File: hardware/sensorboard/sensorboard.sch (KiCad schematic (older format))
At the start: 25 parts, among them P1 PWR, P2 PROG, U1 ESP-07v2, U2 LMR16006Y, U3 BME280

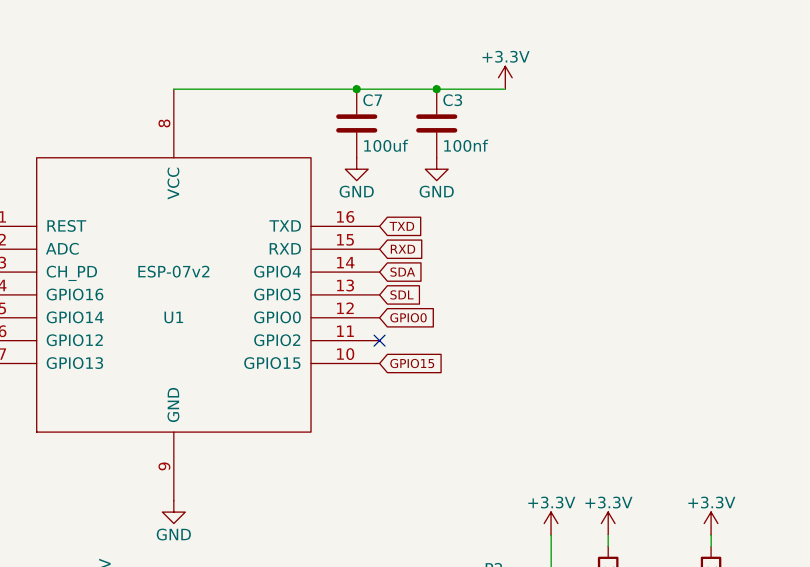
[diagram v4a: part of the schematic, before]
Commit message: Fix sensor placement and improve silkscreens
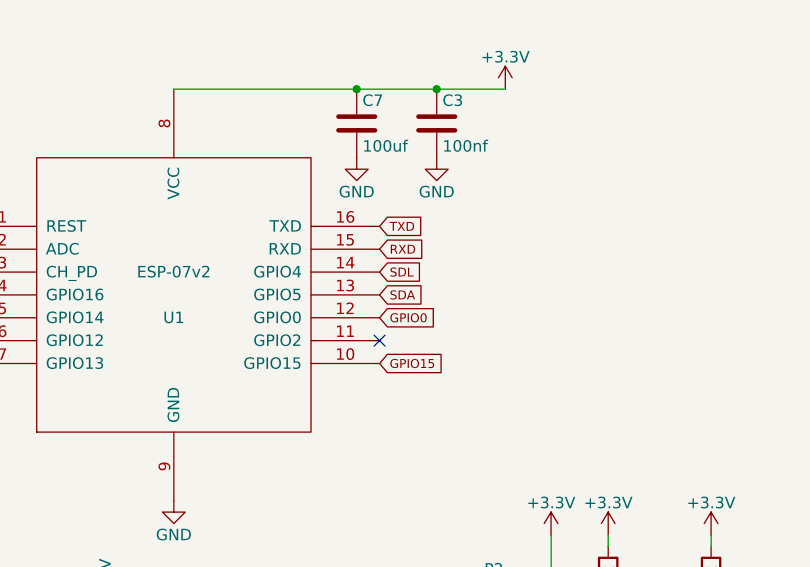
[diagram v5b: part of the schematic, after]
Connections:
- net SDA: now also U1.13 (GPIO5); no longer U1.14 (GPIO4)
- net SDL: now also U1.14 (GPIO4); no longer U1.13 (GPIO5)
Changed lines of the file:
@@
 $EndComp
 $Comp
-L GND #PWR22
+L GND #PWR01
 U 1 1 55FE3581
 P 3350 2700
-F 0 "#PWR22" H 3350 2450 50  0001 C CNN
+F 0 "#PWR01" H 3350 2450 50  0001 C CNN
 F 1 "GND" H 3350 2550 50  0000 C CNN
 F 2 "" H 3350 2700 60  0000 C CNN
@@
 $EndComp
 $Comp
-L +6V #PWR1
+L +6V #PWR02
 U 1 1 55FE36BB
 P 600 5000
-F 0 "#PWR1" H 600 4850 50  0001 C CNN
+F 0 "#PWR02" H 600 4850 50  0001 C CNN
 F 1 "+6V" H 600 5140 50  0000 C CNN
 F 2 "" H 600 5000 60  0000 C CNN
@@
 $EndComp
 $Comp
-L GND #PWR2
+L GND #PWR03
 U 1 1 55FE36DF
 P 600 5100
-F 0 "#PWR2" H 600 4850 50  0001 C CNN
+F 0 "#PWR03" H 600 4850 50  0001 C CNN
 F 1 "GND" H 600 4950 50  0000 C CNN
 F 2 "" H 600 5100 60  0000 C CNN
@@
 $EndComp
 $Comp
-L GND #PWR7
+L GND #PWR04
 U 1 1 55FE3994
 P 1300 600
-F 0 "#PWR7" H 1300 350 50  0001 C CNN
+F 0 "#PWR04" H 1300 350 50  0001 C CNN
 F 1 "GND" H 1300 450 50  0000 C CNN
 F 2 "" H 1300 600 60  0000 C CNN
@@
 $EndComp
 $Comp
-L +3.3V #PWR28
+L +3.3V #PWR05
 U 1 1 55FE3BCB
 P 4800 900
-F 0 "#PWR28" H 4800 750 50  0001 C CNN
+F 0 "#PWR05" H 4800 750 50  0001 C CNN
 F 1 "+3.3V" H 4800 1040 50  0000 C CNN
 F 2 "" H 4800 900 60  0000 C CNN
@@
 $EndComp
 $Comp
-L GND #PWR26
+L GND #PWR06
 U 1 1 55FE3BE8
 P 4500 1200
-F 0 "#PWR26" H 4500 950 50  0001 C CNN
+F 0 "#PWR06" H 4500 950 50  0001 C CNN
 F 1 "GND" H 4500 1050 50  0000 C CNN
 F 2 "" H 4500 1200 60  0000 C CNN
@@
 CH_PD
 $Comp
-L +3.3V #PWR19
+L +3.3V #PWR07
 U 1 1 55FE58BB
 P 3050 3200
-F 0 "#PWR19" H 3050 3050 50  0001 C CNN
+F 0 "#PWR07" H 3050 3050 50  0001 C CNN
 F 1 "+3.3V" V 3050 3340 50  0000 C CNN
 F 2 "" H 3050 3200 60  0000 C CNN
@@
 $EndComp
 $Comp
-L GND #PWR21
+L GND #PWR08
 U 1 1 55FE59ED
 P 3300 3650
-F 0 "#PWR21" H 3300 3400 50  0001 C CNN
+F 0 "#PWR08" H 3300 3400 50  0001 C CNN
 F 1 "GND" H 3300 3500 50  0000 C CNN
 F 2 "" H 3300 3650 60  0000 C CNN
@@
 RXD
 $Comp
-L GND #PWR27
+L GND #PWR09
 U 1 1 55FF1EBD
 P 4500 3500
-F 0 "#PWR27" H 4500 3250 50  0001 C CNN
+F 0 "#PWR09" H 4500 3250 50  0001 C CNN
 F 1 "GND" H 4500 3350 50  0000 C CNN
 F 2 "" H 4500 3500 60  0000 C CNN
@@
 $EndComp
 $Comp
-L +3.3V #PWR29
+L +3.3V #PWR010
 U 1 1 55FF1FBC
 P 5000 2850
-F 0 "#PWR29" H 5000 2700 50  0001 C CNN
+F 0 "#PWR010" H 5000 2700 50  0001 C CNN
 F 1 "+3.3V" H 5000 2990 50  0000 C CNN
 F 2 "" H 5000 2850 60  0000 C CNN
@@
 $EndComp
 $Comp
-L +3.3V #PWR30
+L +3.3V #PWR011
 U 1 1 55FF2085
 P 5250 2850
-F 0 "#PWR30" H 5250 2700 50  0001 C CNN
+F 0 "#PWR011" H 5250 2700 50  0001 C CNN
 F 1 "+3.3V" H 5250 2990 50  0000 C CNN
 F 2 "" H 5250 2850 60  0000 C CNN
@@
 $EndComp
 $Comp
-L +3.3V #PWR31
+L +3.3V #PWR012
 U 1 1 55FF24C3
 P 5700 2850
-F 0 "#PWR31" H 5700 2700 50  0001 C CNN
+F 0 "#PWR012" H 5700 2700 50  0001 C CNN
 F 1 "+3.3V" H 5700 2990 50  0000 C CNN
 F 2 "" H 5700 2850 60  0000 C CNN
@@
 ADC_IN
 $Comp
-L GND #PWR12
+L GND #PWR013
 U 1 1 562D40D4
 P 1950 1250
-F 0 "#PWR12" H 1950 1000 50  0001 C CNN
+F 0 "#PWR013" H 1950 1000 50  0001 C CNN
 F 1 "GND" H 1950 1100 50  0000 C CNN
 F 2 "" H 1950 1250 60  0000 C CNN
@@
 $EndComp
 $Comp
-L +6V #PWR11
+L +6V #PWR014
 U 1 1 562D410C
 P 1950 650
-F 0 "#PWR11" H 1950 500 50  0001 C CNN
+F 0 "#PWR014" H 1950 500 50  0001 C CNN
 F 1 "+6V" H 1950 790 50  0000 C CNN
 F 2 "" H 1950 650 60  0000 C CNN
@@
 $EndComp
 $Comp
-L GND #PWR17
+L GND #PWR015
 U 1 1 56D21A8C
 P 2300 5000
-F 0 "#PWR17" H 2300 4750 50  0001 C CNN
+F 0 "#PWR015" H 2300 4750 50  0001 C CNN
 F 1 "GND" H 2300 4850 50  0000 C CNN
 F 2 "" H 2300 5000 60  0000 C CNN
@@
 $EndComp
 $Comp
-L GND #PWR3
+L GND #PWR016
 U 1 1 56D21D41
 P 900 5700
-F 0 "#PWR3" H 900 5450 50  0001 C CNN
+F 0 "#PWR016" H 900 5450 50  0001 C CNN
 F 1 "GND" H 900 5550 50  0000 C CNN
 F 2 "" H 900 5700 60  0000 C CNN
@@
 $EndComp
 $Comp
-L GND #PWR18
+L GND #PWR017
 U 1 1 56D2214B
 P 2600 5000
-F 0 "#PWR18" H 2600 4750 50  0001 C CNN
+F 0 "#PWR017" H 2600 4750 50  0001 C CNN
 F 1 "GND" H 2600 4850 50  0000 C CNN
 F 2 "" H 2600 5000 60  0000 C CNN
@@
 $EndComp
 $Comp
-L +3.3V #PWR24
+L +3.3V #PWR018
 U 1 1 56D22840
 P 3650 4700
-F 0 "#PWR24" H 3650 4550 50  0001 C CNN
+F 0 "#PWR018" H 3650 4550 50  0001 C CNN
 F 1 "+3.3V" H 3650 4840 50  0000 C CNN
 F 2 "" H 3650 4700 60  0000 C CNN
@@
 $EndComp
 $Comp
-L GND #PWR23
+L GND #PWR019
 U 1 1 56D228E6
 P 3450 5000
-F 0 "#PWR23" H 3450 4750 50  0001 C CNN
+F 0 "#PWR019" H 3450 4750 50  0001 C CNN
 F 1 "GND" H 3450 4850 50  0000 C CNN
 F 2 "" H 3450 5000 60  0000 C CNN
@@
 $EndComp
 $Comp
-L GND #PWR20
+L GND #PWR020
 U 1 1 56D22C06
 P 3100 5500
-F 0 "#PWR20" H 3100 5250 50  0001 C CNN
+F 0 "#PWR020" H 3100 5250 50  0001 C CNN
 F 1 "GND" H 3100 5350 50  0000 C CNN
 F 2 "" H 3100 5500 60  0000 C CNN
@@
 $EndComp
 NoConn ~ 2450 2100
+Text GLabel 4250 1800 2    39   Input ~ 0
+SDA
 Text GLabel 4250 1700 2    39   Input ~ 0
-SDA
-Text GLabel 4250 1800 2    39   Input ~ 0
 SDL
 Text GLabel 2450 1800 0    39   Input ~ 0
@@
 $EndComp
 $Comp
-L GND #PWR9
+L GND #PWR021
 U 1 1 570209C8
 P 1600 3650
-F 0 "#PWR9" H 1600 3400 50  0001 C CNN
+F 0 "#PWR021" H 1600 3400 50  0001 C CNN
 F 1 "GND" H 1600 3500 50  0000 C CNN
 F 2 "" H 1600 3650 60  0000 C CNN
@@
 $EndComp
 $Comp
-L GND #PWR14
+L GND #PWR022
 U 1 1 57020ED6
 P 2000 3650
-F 0 "#PWR14" H 2000 3400 50  0001 C CNN
+F 0 "#PWR022" H 2000 3400 50  0001 C CNN
 F 1 "GND" H 2000 3500 50  0000 C CNN
 F 2 "" H 2000 3650 60  0000 C CNN
@@
 $EndComp
 $Comp
-L +3.3V #PWR4
+L +3.3V #PWR023
 U 1 1 57021047
 P 1000 3950
-F 0 "#PWR4" H 1000 3800 50  0001 C CNN
+F 0 "#PWR023" H 1000 3800 50  0001 C CNN
 F 1 "+3.3V" V 1000 4090 50  0000 C CNN
 F 2 "" H 1000 3950 60  0000 C CNN
@@
 $EndComp
 $Comp
-L +3.3V #PWR16
+L +3.3V #PWR024
 U 1 1 57021094
 P 2300 3950
-F 0 "#PWR16" H 2300 3800 50  0001 C CNN
+F 0 "#PWR024" H 2300 3800 50  0001 C CNN
 F 1 "+3.3V" V 2300 4090 50  0000 C CNN
 F 2 "" H 2300 3950 60  0000 C CNN
@@
 $EndComp
 $Comp
-L +3.3V #PWR8
+L +3.3V #PWR025
 U 1 1 570216D8
 P 1600 2450
-F 0 "#PWR8" H 1600 2300 50  0001 C CNN
+F 0 "#PWR025" H 1600 2300 50  0001 C CNN
 F 1 "+3.3V" V 1600 2590 50  0000 C CNN
 F 2 "" H 1600 2450 60  0000 C CNN
@@
 $EndComp
 $Comp
-L GND #PWR6
+L GND #PWR026
 U 1 1 57021725
 P 1200 2650
-F 0 "#PWR6" H 1200 2400 50  0001 C CNN
+F 0 "#PWR026" H 1200 2400 50  0001 C CNN
 F 1 "GND" H 1200 2500 50  0000 C CNN
 F 2 "" H 1200 2650 60  0000 C CNN
@@
 SDL
 $Comp
-L +3.3V #PWR10
+L +3.3V #PWR027
 U 1 1 57021EEC
 P 1800 1900
-F 0 "#PWR10" H 1800 1750 50  0001 C CNN
+F 0 "#PWR027" H 1800 1750 50  0001 C CNN
 F 1 "+3.3V" V 1800 2040 50  0000 C CNN
 F 2 "" H 1800 1900 60  0000 C CNN
@@
 $EndComp
 $Comp
-L +3.3V #PWR13
+L +3.3V #PWR028
 U 1 1 57021F6F
 P 2000 1900
-F 0 "#PWR13" H 2000 1750 50  0001 C CNN
+F 0 "#PWR028" H 2000 1750 50  0001 C CNN
 F 1 "+3.3V" V 2000 2040 50  0000 C CNN
 F 2 "" H 2000 1900 60  0000 C CNN
@@
 Connection ~ 2000 2150
 $Comp
-L GND #PWR5
+L GND #PWR029
 U 1 1 57022E9C
 P 1150 4150
-F 0 "#PWR5" H 1150 3900 50  0001 C CNN
+F 0 "#PWR029" H 1150 3900 50  0001 C CNN
 F 1 "GND" H 1150 4000 50  0000 C CNN
 F 2 "" H 1150 4150 60  0000 C CNN
@@
 Connection ~ 2150 3950
 $Comp
-L GND #PWR15
+L GND #PWR030
 U 1 1 5702315A
 P 2150 4150
-F 0 "#PWR15" H 2150 3900 50  0001 C CNN
+F 0 "#PWR030" H 2150 3900 50  0001 C CNN
 F 1 "GND" H 2150 4000 50  0000 C CNN
 F 2 "" H 2150 4150 60  0000 C CNN
@@
 $EndComp
 $Comp
-L GND #PWR25
+L GND #PWR031
 U 1 1 57023490
 P 4150 1200
-F 0 "#PWR25" H 4150 950 50  0001 C CNN
+F 0 "#PWR031" H 4150 950 50  0001 C CNN
 F 1 "GND" H 4150 1050 50  0000 C CNN
 F 2 "" H 4150 1200 60  0000 C CNN

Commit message: Fixed soldermask around the bme280
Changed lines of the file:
@@
 $EndComp
 Wire Wire Line
-	600  5000 1300 5000
+	600  5000 900  5000
 Wire Wire Line
-	3350 900  4800 900
+	900  5000 1050 5000
+Wire Wire Line
+	1050 5000 1300 5000
+Wire Wire Line
+	3350 900  4150 900
+Wire Wire Line
+	4150 900  4500 900
+Wire Wire Line
+	4500 900  4800 900
 Connection ~ 4500 900
 Wire Wire Line
@@
 Connection ~ 5250 3200
 Wire Wire Line
-	5000 3200 5400 3200
+	5000 3200 5250 3200
+Wire Wire Line
+	5250 3200 5400 3200
 Connection ~ 5250 3300
 Connection ~ 5700 3300
@@
 	5250 2900 5250 2850
 Wire Wire Line
-	5000 3300 5800 3300
+	5000 3300 5250 3300
+Wire Wire Line
+	5250 3300 5700 3300
+Wire Wire Line
+	5700 3300 5800 3300
 Wire Wire Line
 	5250 3300 5250 3400
@@
 Connection ~ 3100 5300
 Wire Wire Line
-	3100 4700 3650 4700
+	3100 4700 3450 4700
+Wire Wire Line
+	3450 4700 3650 4700
 Connection ~ 3450 4700
 Wire Wire Line
-	2600 4400 2600 4800
+	2600 4400 2600 4700
+Wire Wire Line
+	2600 4700 2600 4800
 Wire Wire Line
 	1400 3950 1400 3650
 Wire Wire Line
-	1000 3950 1400 3950
+	1000 3950 1150 3950
+Wire Wire Line
+	1150 3950 1400 3950
 Wire Wire Line
 	1800 3650 1800 3950
 Wire Wire Line
-	1800 3950 2300 3950
+	1800 3950 2150 3950
+Wire Wire Line
+	2150 3950 2300 3950
 Wire Wire Line
 	1200 2650 1200 2450
@@
 	1200 2450 1400 2450
 Wire Wire Line
-	1800 2450 1800 2100
+	1800 2450 1800 2150
+Wire Wire Line
+	1800 2150 1800 2100
 Wire Wire Line
 	1400 2150 1800 2150
 Connection ~ 1800 2150
 Wire Wire Line
-	2000 2450 2000 2100
+	2000 2450 2000 2150
+Wire Wire Line
+	2000 2150 2000 2100
 Wire Wire Line
 	2100 2150 2000 2150

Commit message: Fixed some silkscreens, added BOM.
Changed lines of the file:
@@
 $EndComp
 Wire Wire Line
-	600  5000 900  5000
+	600  5000 1300 5000
 Wire Wire Line
-	900  5000 1050 5000
-Wire Wire Line
-	1050 5000 1300 5000
-Wire Wire Line
-	3350 900  4150 900
-Wire Wire Line
-	4150 900  4500 900
-Wire Wire Line
-	4500 900  4800 900
+	3350 900  4800 900
 Connection ~ 4500 900
 Wire Wire Line
@@
 Connection ~ 5250 3200
 Wire Wire Line
-	5000 3200 5250 3200
-Wire Wire Line
-	5250 3200 5400 3200
+	5000 3200 5400 3200
 Connection ~ 5250 3300
 Connection ~ 5700 3300
@@
 	5250 2900 5250 2850
 Wire Wire Line
-	5000 3300 5250 3300
-Wire Wire Line
-	5250 3300 5700 3300
-Wire Wire Line
-	5700 3300 5800 3300
+	5000 3300 5800 3300
 Wire Wire Line
 	5250 3300 5250 3400
@@
 Connection ~ 3100 5300
 Wire Wire Line
-	3100 4700 3450 4700
-Wire Wire Line
-	3450 4700 3650 4700
+	3100 4700 3650 4700
 Connection ~ 3450 4700
 Wire Wire Line
-	2600 4400 2600 4700
-Wire Wire Line
-	2600 4700 2600 4800
+	2600 4400 2600 4800
 Wire Wire Line
 	1400 3950 1400 3650
 Wire Wire Line
-	1000 3950 1150 3950
-Wire Wire Line
-	1150 3950 1400 3950
+	1000 3950 1400 3950
 Wire Wire Line
 	1800 3650 1800 3950
 Wire Wire Line
-	1800 3950 2150 3950
-Wire Wire Line
-	2150 3950 2300 3950
+	1800 3950 2300 3950
 Wire Wire Line
 	1200 2650 1200 2450
@@
 	1200 2450 1400 2450
 Wire Wire Line
-	1800 2450 1800 2150
-Wire Wire Line
-	1800 2150 1800 2100
+	1800 2100 1800 2450
 Wire Wire Line
 	1400 2150 1800 2150
 Connection ~ 1800 2150
 Wire Wire Line
-	2000 2450 2000 2150
-Wire Wire Line
-	2000 2150 2000 2100
+	2000 2100 2000 2450
 Wire Wire Line
 	2100 2150 2000 2150
